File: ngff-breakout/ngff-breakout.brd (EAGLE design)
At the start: 90 x 80 mm, 77 parts, among them U2 LD1085D2T33R, X1 PINHD-2X4, X7 694108106102, X9 ZX360D-B-10P(30), Y4 MHF4, Y5 MHF4, Y6 MHF4

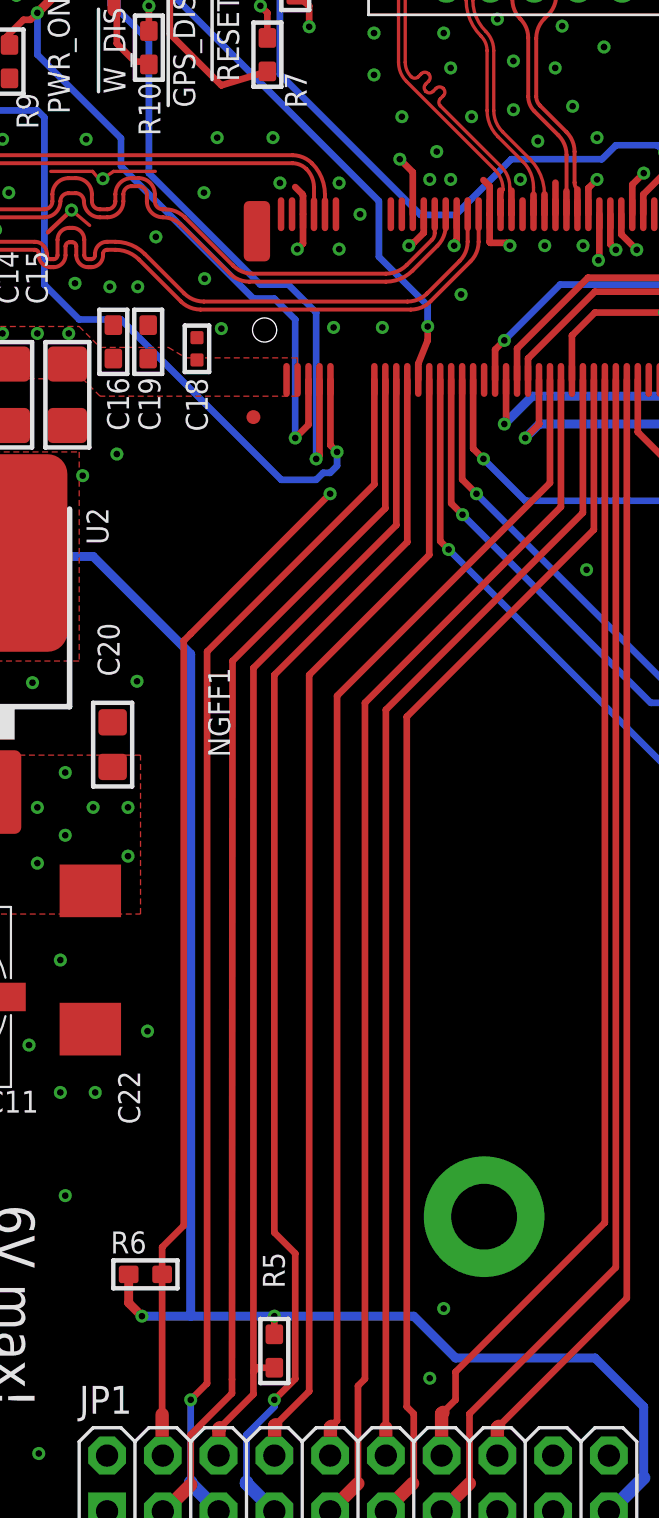
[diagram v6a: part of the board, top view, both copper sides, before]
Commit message: ngff: repair M.2/NGFF footprint (see SYS#4661)
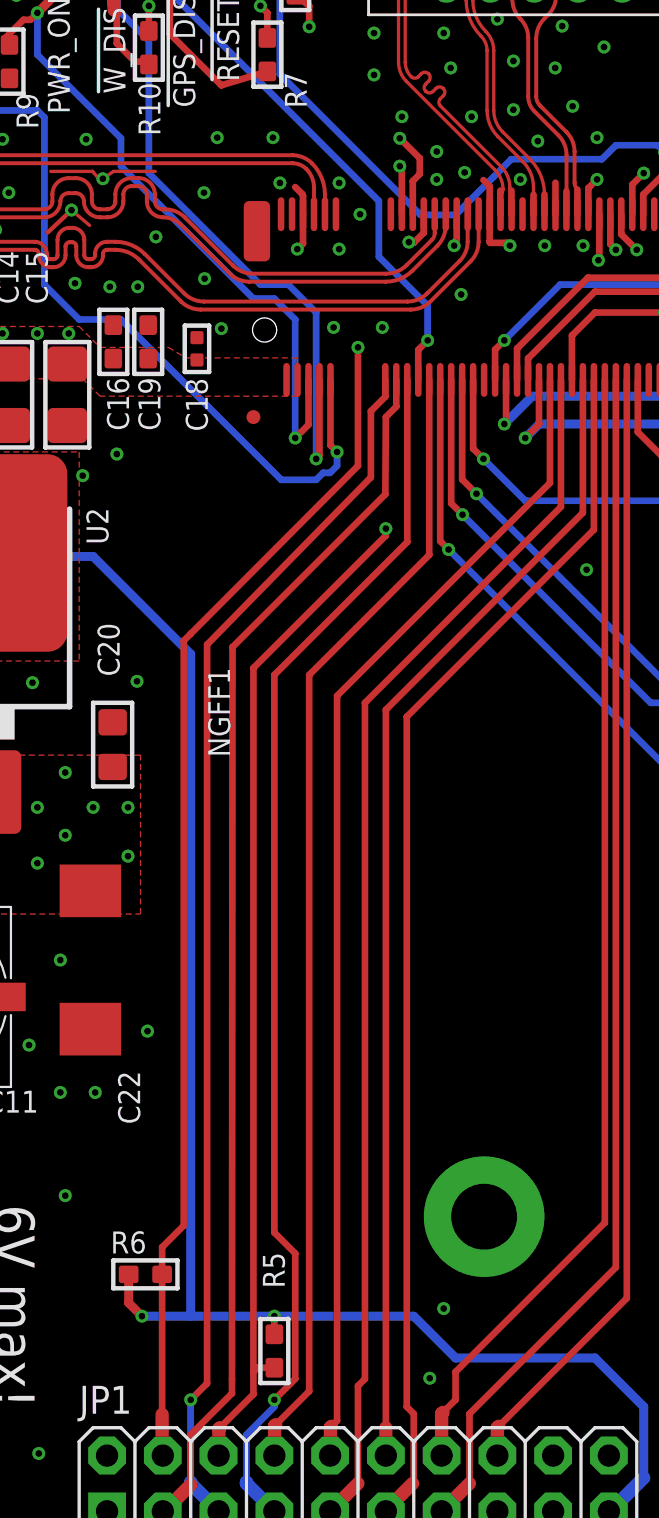
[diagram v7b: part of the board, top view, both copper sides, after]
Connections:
- net GND: now also NGFF1.45
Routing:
- net !WAKE_ON_WWAN: track 53.4 -> 66.0 mm, vias 0 -> 2
- net !BODY_SAR: track 66.8 -> 68.7 mm

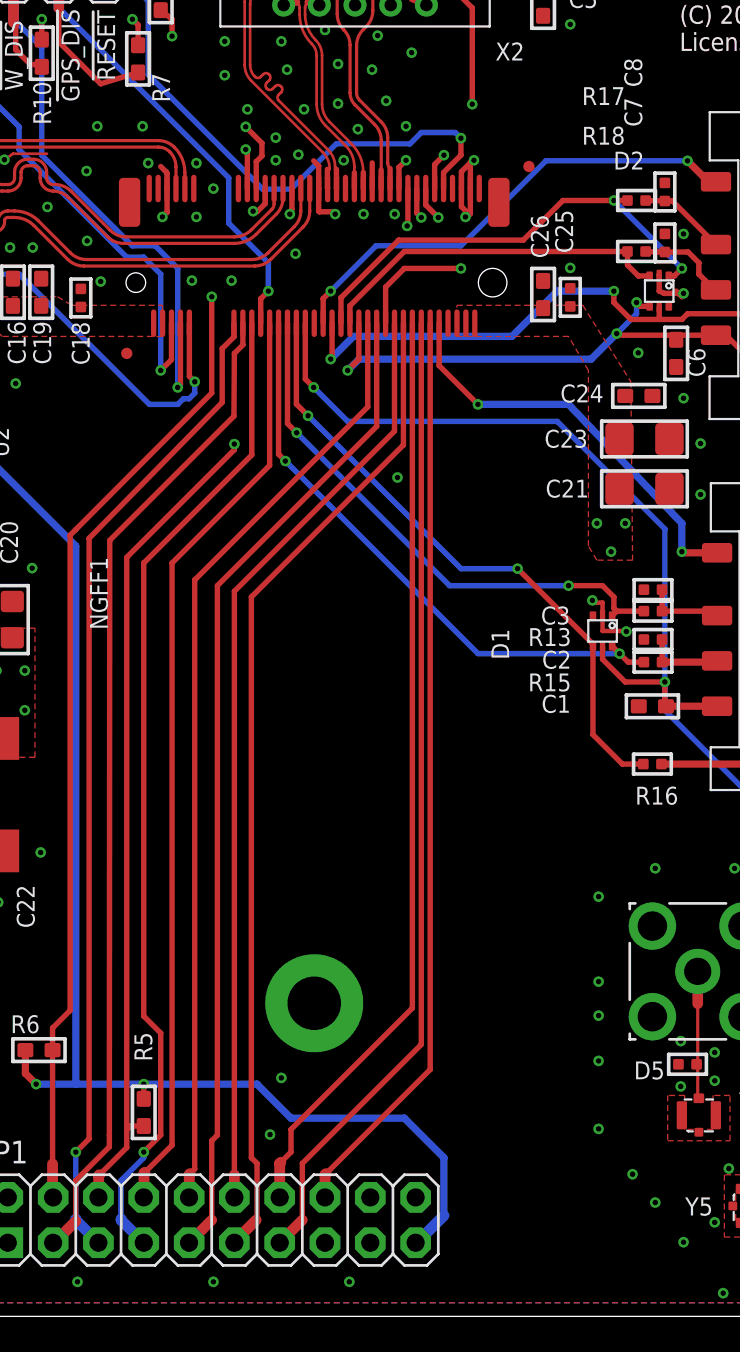
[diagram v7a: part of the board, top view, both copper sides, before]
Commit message: ngff: route all four ANTCTLn signals on bottom layer (fixes OS#4187)
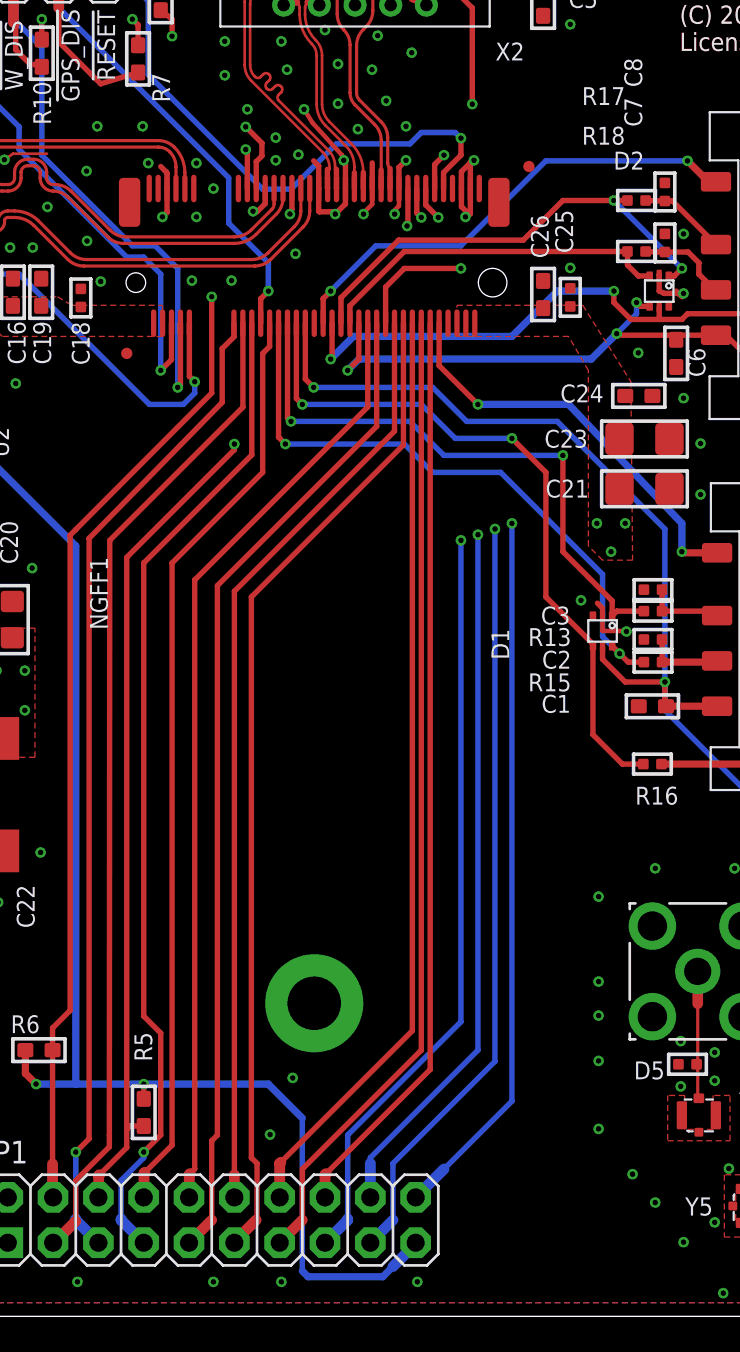
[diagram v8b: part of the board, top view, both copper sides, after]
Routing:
- net GND: track 39.8 -> 49.2 mm
- net _USIM1_DATA: track 35.3 -> 39.2 mm
- net _USIM1_CLK: track 30.7 -> 33.6 mm
- net VCC_1V8: track 134.5 -> 136.1 mm
- net _!USIM1_RESET: track 33.2 -> 34.7 mm
- net ANTCTL3: track 65.8 -> 64.7 mm, vias 1 -> 2
- net ANTCTL0: track 64.2 -> 63.5 mm, vias 1 -> 2
- net ANTCTL2: track 64.4 -> 63.9 mm, vias 1 -> 2
- net ANTCTL1: track 60.7 -> 60.5 mm, vias 1 -> 3
